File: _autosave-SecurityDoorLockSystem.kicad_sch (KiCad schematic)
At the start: 12 parts, among them J1 Power In, J2 Servo, J3 RFID-RC522, J4 R307s, U1 ESP32-DEVKIT-V1, U2 L7805

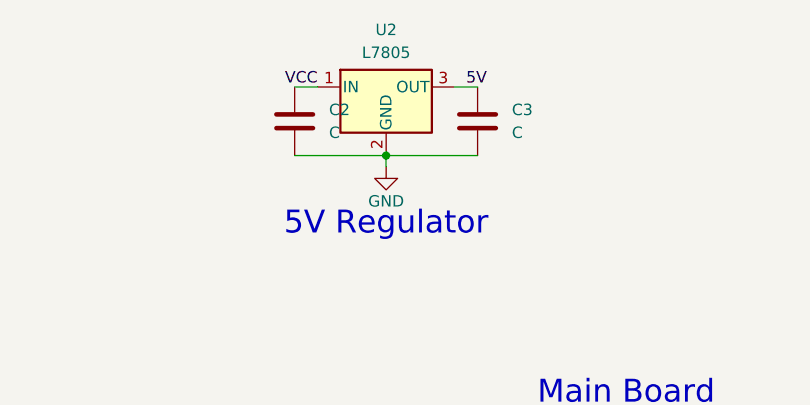
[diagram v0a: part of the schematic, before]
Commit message: version 2
increased track width
added voltage regulator
corrected tht-friendly error
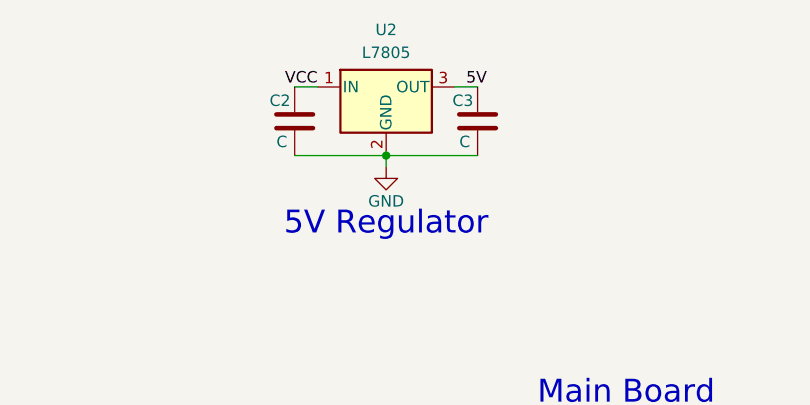
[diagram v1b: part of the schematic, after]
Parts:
- C3: footprint (none) -> Capacitor_THT:C_Radial_D5.0mm_H7.0mm_P2.00mm
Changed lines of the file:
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@@
+	)
+	(symbol
+		(lib_id "Device:C")
+		(at 151.13 45.72 0)
+		(unit 1)
+		(exclude_from_sim no)
+		(in_bom yes)
+		(on_board yes)
+		(dnp no)
+		(property "Reference" "C3"
+			(at 148.336 43.434 0)
+			(effects
+				(font
+					(size 1.27 1.27)
+				)
+				(justify left)
+			)
+		)
+		(property "Value" "C"
+			(at 149.098 48.006 0)
+			(effects
+				(font
+					(size 1.27 1.27)
+				)
+				(justify left)
+			)
+		)
+		(property "Footprint" "Capacitor_THT:C_Radial_D5.0mm_H7.0mm_P2.00mm"
+			(at 152.0952 49.53 0)
+			(effects
+				(font
+					(size 1.27 1.27)
+				)
+				(hide yes)
+			)
+		)
+		(property "Datasheet" "~"
+			(at 151.13 45.72 0)
+			(effects
+				(font
+					(size 1.27 1.27)
+				)
+				(hide yes)
+			)
+		)
+		(property "Description" "Unpolarized capacitor"
+			(at 151.13 45.72 0)
+			(effects
+				(font
+					(size 1.27 1.27)
+				)
+				(hide yes)
+			)
+		)
+		(pin "2"
+		)
+		(pin "1"
+		)
+		(instances
+			(project "SecurityDoorLockSystem"
+				(path "/8711d31f-b08a-48db-983d-0d74003b609c"
+					(reference "C3")
+					(unit 1)
+				)
+			)
+		)
 	)
 	(symbol
@@
 		(on_board yes)
 		(dnp no)
-		(fields_autoplaced yes)
 		(property "Reference" "C2"
-			(at 134.62 44.4499 0)
+			(at 128.016 43.434 0)
 			(effects
 				(font
@@
 		)
 		(property "Value" "C"
-			(at 134.62 46.9899 0)
+			(at 128.778 48.006 0)
 			(effects
 				(font
@@
 					(unit 1)
 				)
-			)
-		)
-	)
-	(symbol
-		(lib_id "Device:C")
-		(at 151.13 45.72 0)
-		(unit 1)
-		(exclude_from_sim no)
-		(in_bom yes)
-		(on_board yes)
-		(dnp no)
-		(fields_autoplaced yes)
-		(property "Reference" "C3"
-			(at 154.94 44.4499 0)
-			(effects
-				(font
-					(size 1.27 1.27)
-				)
-				(justify left)
-			)
-		)
-		(property "Value" "C"
-			(at 154.94 46.9899 0)
-			(effects
-				(font
-					(size 1.27 1.27)
-				)
-				(justify left)
-			)
-		)
-		(property "Footprint" ""
-			(at 152.0952 49.53 0)
-			(effects
-				(font
-					(size 1.27 1.27)
-				)
-				(hide yes)
-			)
-		)
-		(property "Datasheet" "~"
-			(at 151.13 45.72 0)
-			(effects
-				(font
-					(size 1.27 1.27)
-				)
-				(hide yes)
-			)
-		)
-		(property "Description" "Unpolarized capacitor"
-			(at 151.13 45.72 0)
-			(effects
-				(font
-					(size 1.27 1.27)
-				)
-				(hide yes)
-			)
-		)
-		(pin "2"
-		)
-		(pin "1"
-		)
-		(instances
-			(project ""
-				(path "/8711d31f-b08a-48db-983d-0d74003b609c"
-					(reference "C3")
-					(unit 1)
-				)
